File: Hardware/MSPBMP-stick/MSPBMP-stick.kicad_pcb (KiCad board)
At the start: 2 copper layers, 50 x 20 mm, 41 parts, among them J1 48037-0001, J2 JTAG, J3 ISP, U1 MCP1700T-3302E/TT, U2 STM32F103CBT6, U3 LM358DR2G, U4 TXS0108EPWR, Y1 8MHz

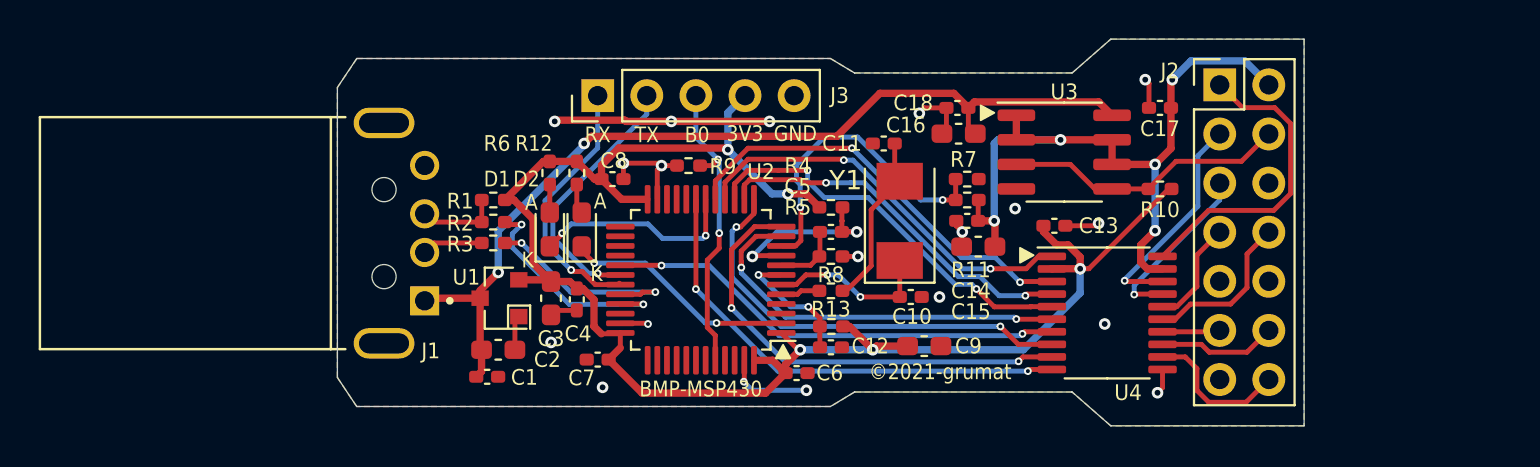
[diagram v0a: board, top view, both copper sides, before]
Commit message: Improved Hardware project in the stick form factor
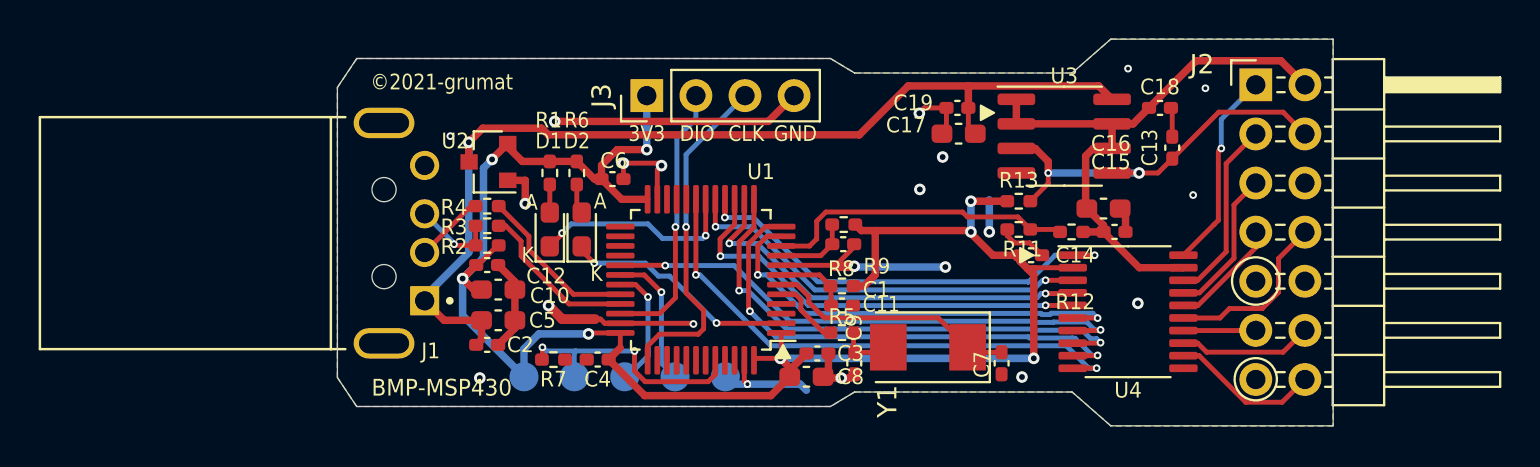
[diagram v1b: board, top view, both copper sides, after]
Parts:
- removed the R5 at (89.0, 62.0)
- removed the R9 at (81.7, 57.3)
- added C13: 100nF, Capacitor_SMD:C_0402_1005Metric_Pad0.74x0.62mm_HandSolder, F.Cu at (106.7, 56.4)
- added NT1: GND-GNDA, NetTie:NetTie-2_SMD_Pad0.5mm, F.Cu at (89.7, 62.5)
- added R11: 4k7, Resistor_SMD:R_0402_1005Metric_Pad0.72x0.64mm_HandSolder, F.Cu at (98.7, 60.6)
- added TP1: 3v3, TestPoint:TestPoint_Pad_D1.5mm, B.Cu at (73.2, 68.3)
- added TP2: BOOT0, TestPoint:TestPoint_Pad_D1.5mm, B.Cu at (75.8, 68.3)
- added TP3: ISP_RX, TestPoint:TestPoint_Pad_D1.5mm, B.Cu at (78.4, 68.3)
- added TP4: ISP_TX, TestPoint:TestPoint_Pad_D1.5mm, B.Cu at (81.0, 68.3)
- added TP5: GND, TestPoint:TestPoint_Pad_D1.5mm, B.Cu at (83.6, 68.3)
- J2: footprint Connector_PinHeader_2.54mm:PinHeader_2x07_P2.54mm_Vertical -> Connector_PinHeader_2.54mm:PinHeader_2x07_P2.54mm_Horizontal
- J3: value ISP -> SWD; footprint Connector_PinHeader_2.54mm:PinHeader_1x05_P2.54mm_Vertical -> Connector_PinHeader_2.54mm:PinHeader_1x04_P2.54mm_Vertical
- R7: value 4k7 -> 100K
- moved R7 23.3 mm to (74.7, 67.4), turned to 180 degrees
- moved C9 11.5 mm to (90.2, 67.6), turned to 270 degrees
- moved C15 7.64 mm to (103.7, 60.8), turned to 0 degrees
- moved R13 7.33 mm to (98.7, 59.2), turned to 180 degrees
- moved U2 7.07 mm to (71.3, 57.1)
- moved C16 6.77 mm to (103.1, 59.6), turned to 0 degrees
- moved Y1 6.70 mm to (94.0, 66.7), turned to 180 degrees
- moved C8 6.30 mm to (87.8, 68.3)
- moved C7 5.82 mm to (97.9, 67.6), turned to 270 degrees
- moved R12 5.64 mm to (101.5, 60.8)
- moved C12 4.96 mm to (71.2, 62.5), turned to 0 degrees
- moved C10 2.77 mm to (71.8, 63.8), turned to 0 degrees
- moved J3 2.54 mm to (79.5, 53.7)
- moved R2 2.37 mm to (71.2, 61.5)
- moved C11 2.23 mm to (89.6, 64.6)
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- renumbered C5 to C1, C3 to C10, C12 to C11, C4 to C12, C13 to C14, C14 to C15, C15 to C16, C16 to C17, C17 to C18, C18 to C19, C1 to C2, C6 to C3, C7 to C4, C2 to C5, C8 to C6, C10 to C7, C9 to C8, C11 to C9, R6 to R1, R11 to R12, R10 to R13, R1 to R2, R2 to R3, R3 to R4, R8 to R5, R12 to R6, R13 to R8, R4 to R9, U2 to U1, U1 to U2
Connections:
- J3 pad 1: /ISP_RX -> +3V3
- J3 pad 2: /ISP_TX -> /SWDIO
- J3 pad 3: /BOOT0 -> /SWCLK
- J3 pad 4: +3V3 -> GND
- R7 pad 1: /VREF2 -> GND
- R7 pad 2: GND -> /BOOT0
- U1 pad 34: Net-(U2-Pad34) -> /SWDIO
- U1 pad 37: Net-(U2-Pad37) -> /SWCLK
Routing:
- net GND: track 36.2 -> 56.1 mm, vias 19 -> 21
- net /SWCLK: track 0.00 -> 17.7 mm, vias 0 -> 1
- net /SWDIO: track 0.00 -> 14.1 mm, vias 0 -> 1
- net /ISP_RX: track 13.7 -> 6.42 mm
- net +3V3: track 90.9 -> 97.8 mm, vias 5 -> 8
- net /ISP_TX: track 14.0 -> 7.16 mm
- net /VCC_TOOL: track 37.8 -> 31.1 mm, vias 5 -> 0
- net Net-(C9-Pad1): track 9.06 -> 2.90 mm
- net /TVCC: track 14.8 -> 20.8 mm, vias 0 -> 2
- net /TTDO: track 16.1 -> 10.4 mm, vias 0 -> 1
- net +3.3VA: track 9.49 -> 3.90 mm, vias 2 -> 0
- net +5V: track 48.0 -> 53.2 mm, vias 2 -> 1
- net /OSC_OUT: track 8.70 -> 13.0 mm, vias 2 -> 0
- net /JRST: track 23.9 -> 27.7 mm
- net /JRXD: track 22.6 -> 26.3 mm
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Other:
- board size 50 x 20 mm -> 51.5 x 20 mm
- net class Power: trace_width 0.4 -> 0.387
- board text added: "CLK"
- board text added: "DIO"
- board text removed: "B0"
- board text removed: "RX"
- board text removed: "TX"

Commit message: Schematics and PCB review
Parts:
- added R10: 47K, Resistor_SMD:R_0402_1005Metric_Pad0.72x0.64mm_HandSolder, F.Cu at (104.8, 69.0)
- U2: value MCP1700T-3302E/TT -> LD1117AG-33-AB3-A-R; footprint Package_TO_SOT_SMD:SOT-23 -> Package_TO_SOT_SMD:SOT-89-3
- moved D1 18.0 mm to (92.5, 60.7)
- moved D2 17.8 mm to (94.0, 60.7)
- moved R1 15.3 mm to (89.7, 59.2), turned to 180 degrees
- moved R6 13.8 mm to (89.7, 58.2), turned to 180 degrees
- moved R13 11.7 mm to (108.6, 52.9), turned to 90 degrees
- moved C13 3.63 mm to (107.6, 52.9), turned to 270 degrees
- moved C16 1.79 mm to (104.9, 59.4)
- moved U2 1.66 mm to (72.7, 56.3)
- moved C18 1.55 mm to (106.6, 52.9), turned to 270 degrees
- moved C15 0.90 mm to (104.6, 60.6)
- moved C12 0.89 mm to (72.1, 62.5)
- moved C2 0.89 mm to (72.1, 66.6)
- moved R2 0.89 mm to (72.1, 61.5)
- moved R3 0.89 mm to (72.1, 60.5)
- moved R4 0.89 mm to (72.1, 59.4)
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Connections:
- C18 pad 1: /VCC_TOOL -> +3V3
- J2 pad 2: /VCC_TOOL -> +3V3
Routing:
- net GND: track 56.1 -> 27.3 mm, vias 21 -> 20
- net +3V3: track 97.8 -> 115.4 mm, vias 8 -> 6
- net /VCC_TOOL: track 31.1 -> 20.7 mm
- net /LED_GREEN: track 10.9 -> 14.4 mm
- net /JENA: track 27.9 -> 31.3 mm
- net Net-(D2-Pad2): track 1.55 -> 4.41 mm
- net /TVCC: track 20.8 -> 23.2 mm
- net /LED_RED: track 12.2 -> 13.8 mm
- net /USBP: track 8.41 -> 7.08 mm
- net /USBM: track 8.58 -> 7.29 mm
- net /JTDO: track 23.2 -> 22.0 mm
- net /JRST: track 27.7 -> 28.8 mm
- net Net-(D1-Pad2): track 1.45 -> 2.45 mm
- net /JRXD: track 26.3 -> 27.3 mm
- net /HUSBP: track 4.97 -> 5.86 mm
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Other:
- board text added: "3v3:B0:RX:TX:GND"

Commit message: More Hardware improvements
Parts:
- added RN1: 33, Resistor_SMD:R_Array_Convex_4x0402, F.Cu at (108.2, 60.9)
- added RN2: 33, Resistor_SMD:R_Array_Convex_4x0402, F.Cu at (108.2, 66.0)
- C10, C16, C17, C8: value 4.7uF -> 22uF
- C5: value 4.7uF -> 10uF
- moved C8 12.0 mm to (90.0, 56.5)
- moved C10 4.21 mm to (72.5, 59.5), turned to 180 degrees
- moved R3 2.62 mm to (72.1, 63.1)
- moved R4 2.62 mm to (72.1, 62.1)
- moved R2 2.62 mm to (72.1, 64.1)
- moved C14 2.33 mm to (97.1, 62.5), turned to 180 degrees
- moved U4 2.00 mm to (102.4, 64.7)
- moved C12 1.66 mm to (72.1, 60.8), turned to 180 degrees
- moved C3 0.79 mm to (88.1, 67.8)
- moved C16 0.57 mm to (104.3, 59.4)
- moved R10 0.44 mm to (104.3, 69.0)
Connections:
- U4 pad 12: /TRXD -> Net-(RN2-Pad4)
- U4 pad 13: /TTXD -> Net-(RN2-Pad3)
- U4 pad 14: /TRST -> Net-(RN2-Pad2)
- U4 pad 15: /TTEST -> Net-(RN2-Pad1)
- U4 pad 16: /TTCK -> Net-(RN1-Pad4)
- U4 pad 17: /TTMS -> Net-(RN1-Pad3)
- U4 pad 18: /TTDI -> Net-(RN1-Pad2)
- U4 pad 20: /TTDO -> Net-(RN1-Pad1)
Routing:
- net GND: track 27.3 -> 40.7 mm, vias 20 -> 19
- net +3V3: track 115.4 -> 110.9 mm
- net Net-(RN1-Pad4): track 0.00 -> 4.17 mm
- net Net-(RN1-Pad3): track 0.00 -> 4.17 mm
- net Net-(RN1-Pad2): track 0.00 -> 4.11 mm
- net /TTMS: track 7.72 -> 4.18 mm
- net /TTDI: track 9.55 -> 6.18 mm
- net /TTCK: track 6.13 -> 3.06 mm
- net Net-(RN1-Pad1): track 0.00 -> 3.07 mm
- net /JTMS: track 22.1 -> 19.5 mm
- net /JTCK: track 23.0 -> 20.5 mm
- net /JRXD: track 27.3 -> 24.8 mm
- net Net-(RN2-Pad4): track 0.00 -> 2.49 mm
- net /JTEST: track 22.8 -> 20.3 mm
- net Net-(RN2-Pad1): track 0.00 -> 2.47 mm
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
